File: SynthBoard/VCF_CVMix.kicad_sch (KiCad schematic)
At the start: 22 parts, among them IC1 AS321KTR-G1, J7 Input, Q3 2SA812, Q4 2SC1623(RANGE:300-400), Q7 2SA812

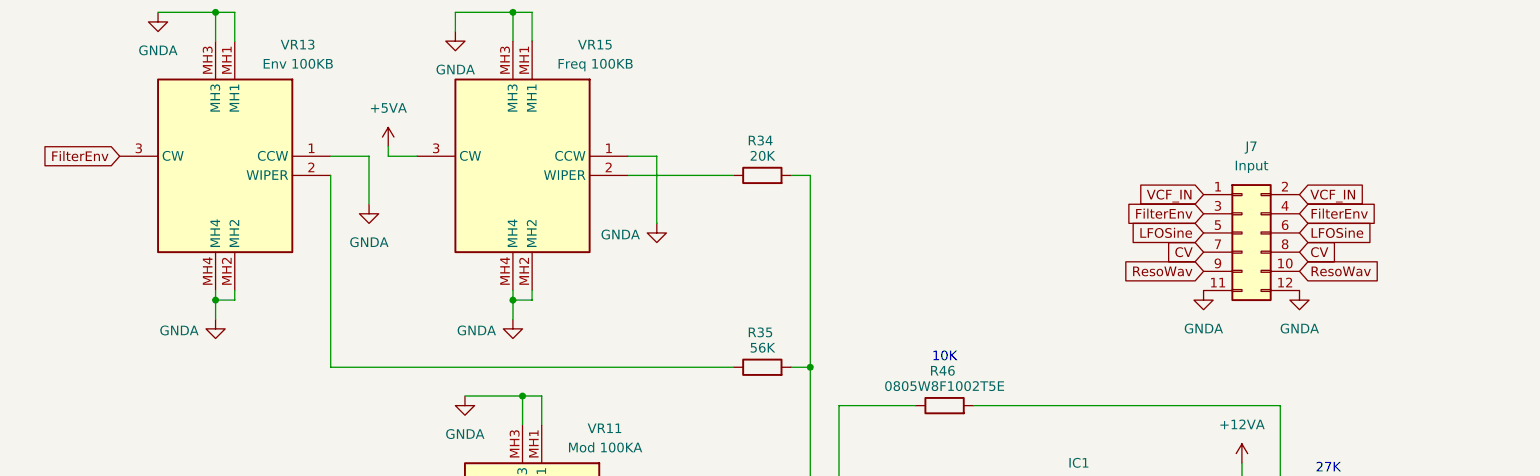
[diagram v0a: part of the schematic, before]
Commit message: SynthBorad
デジタルも配置した
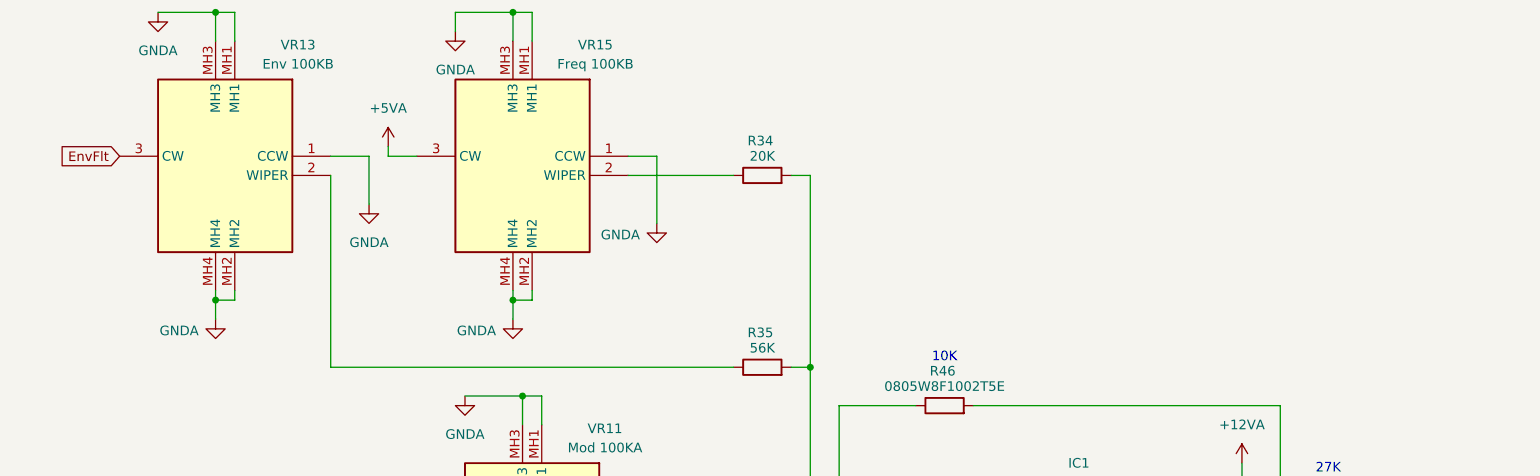
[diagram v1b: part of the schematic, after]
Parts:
- removed J7: Input, Connector_PinSocket_2.54mm:PinSocket_2x06_P2.54mm_Vertical, symbol Connector_Generic:Conn_02x06_Odd_Even
- VR10, VR19: footprint 3362P_1 -> SamacSys_parts:3362P_1
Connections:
- net FilterEnv renamed EnvFlt
